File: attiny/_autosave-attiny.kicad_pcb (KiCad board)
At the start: 2 copper layers, 15.4 x 40.2 mm, 11 parts, among them J1 arduino, J2 esp32, J3 cavalier, J4 Conn_01x01, U1 ATtiny85V-10S

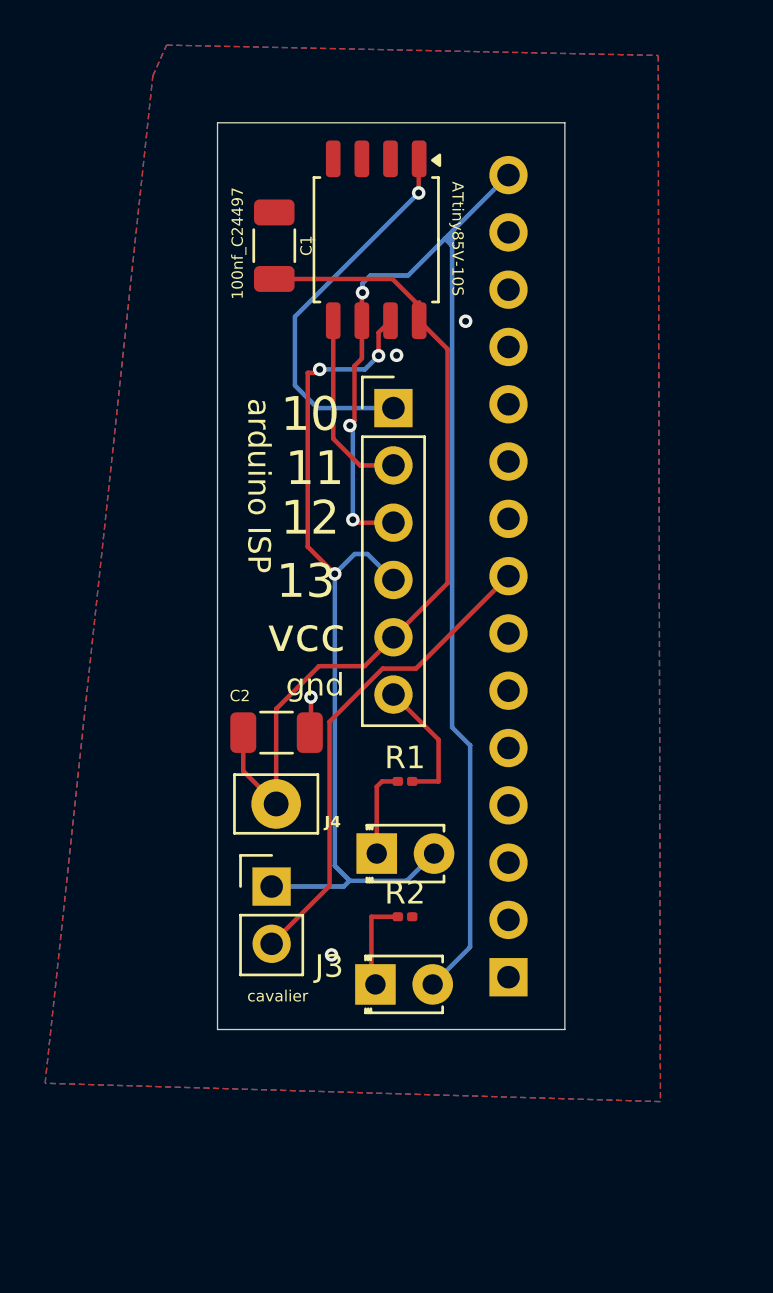
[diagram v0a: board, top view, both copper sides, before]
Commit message: acomposant pour production automatique chez jlcpcb environ 18€ 2 pcb assemblé et 3 non assemblé
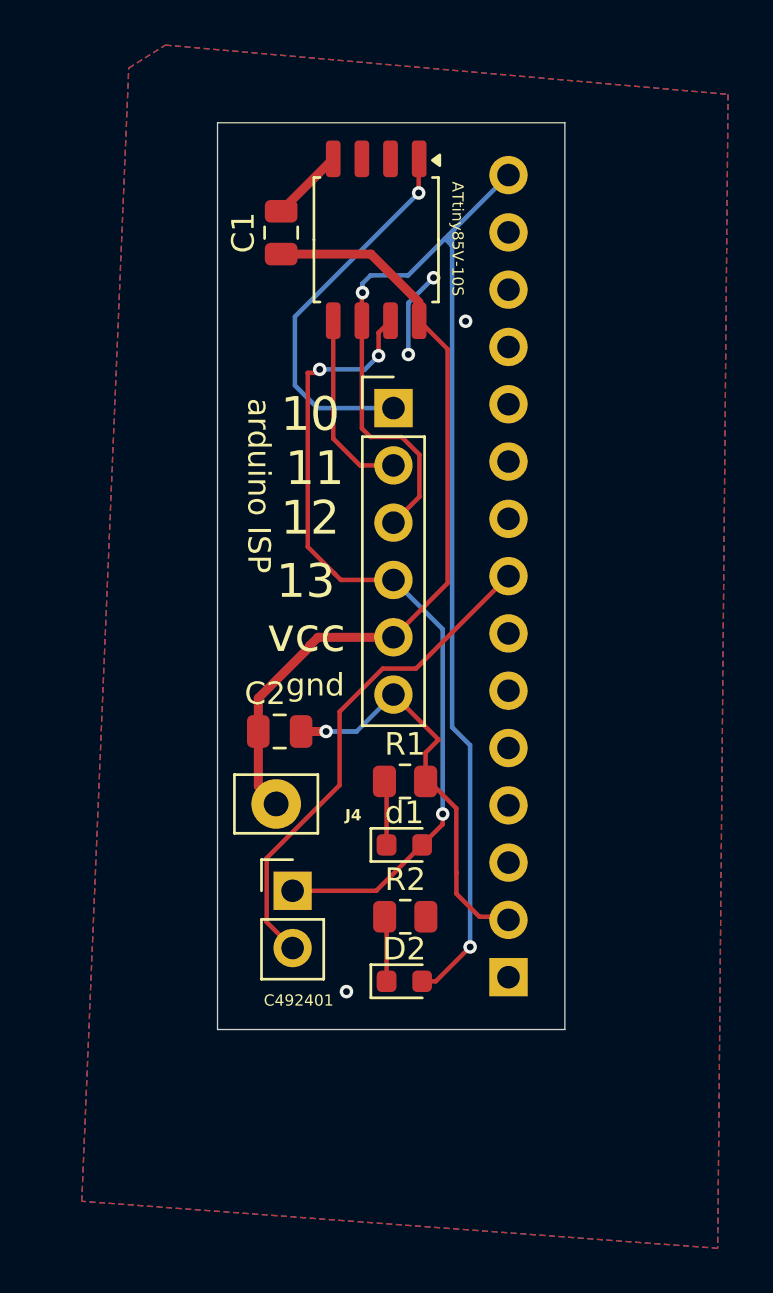
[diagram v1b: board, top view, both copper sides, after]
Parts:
- C1, C2: value 100nf_C24497 -> 100nf_C49678; footprint Capacitor_SMD:C_1206_3216Metric -> Capacitor_SMD:C_0805_2012Metric
- D2: value LED -> LED_C2286; footprint LED_THT:LED_D1.8mm_W3.3mm_H2.4mm -> LED_SMD:LED_0603_1608Metric
- R1: value 12kΩ_C22790 -> 12kΩ_C17444; footprint Resistor_SMD:R_0201_0603Metric -> Resistor_SMD:R_0805_2012Metric
- R2: value 12kΩ _C22790 -> 12kΩ_C17444; footprint Resistor_SMD:R_0201_0603Metric -> Resistor_SMD:R_0805_2012Metric
- arduino1: renamed from J1; value arduino -> C492405
- cavalier1: renamed from J3; value cavalier -> C492401
- d1: renamed from D1; value LED -> LED_C2290; footprint LED_THT:LED_D1.8mm_W3.3mm_H2.4mm -> LED_SMD:LED_0603_1608Metric
- esp32: renamed from J2; value esp32 -> ~
- moved D2 1.29 mm to (152.9, 86.5)
- moved d1 1.28 mm to (152.9, 80.4)
- moved cavalier1 0.95 mm to (147.9, 82.4)
- moved C1 0.65 mm to (147.4, 53.3)
- moved C2 0.15 mm to (147.4, 75.4)
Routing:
- net GND: track 7.89 -> 25.6 mm, vias 4 -> 5
- net VCC: track 38.6 -> 35.7 mm
- net Net-(U1-PB2): track 39.8 -> 37.0 mm
- net Net-(d1-K): track 3.99 -> 2.32 mm
- net Net-(D2-K): track 4.24 -> 2.90 mm
- net Net-(cavalier1-Pin_2): track 21.5 -> 22.3 mm
- net Net-(D2-A): track 57.6 -> 57.4 mm, vias 3 -> 2
